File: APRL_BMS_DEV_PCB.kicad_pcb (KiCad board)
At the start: 4 copper layers, 73 parts, among them J1 Conn_01x04_Pin, J3 Conn_01x02_Pin, J4 Conn_01x08_Pin, J5 Conn_01x01_Pin, Q2 NPN, SW1 SW_SPDT, U1 BQ756506-Q1, U2 STM32F446RCTx, U3 ISO7741DWR, Y1 20MHz

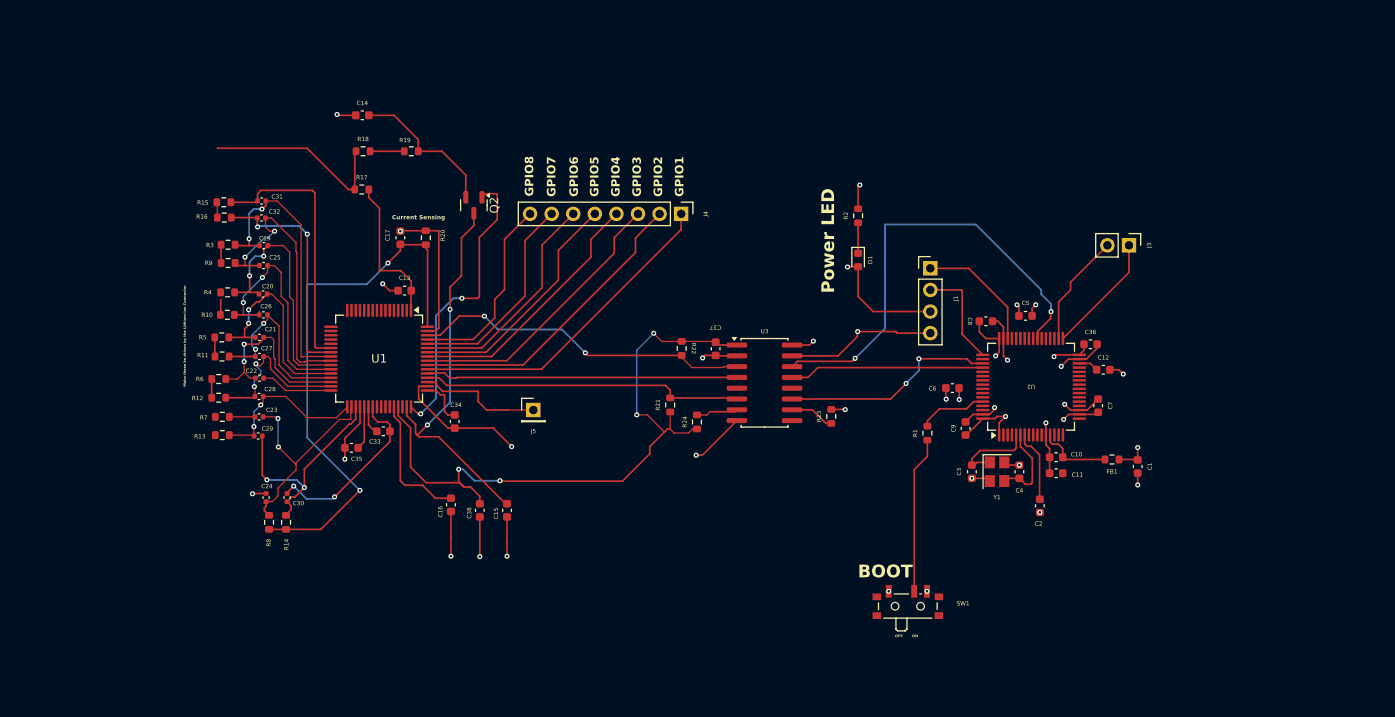
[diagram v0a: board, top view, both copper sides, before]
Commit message: Fixed silkscreen
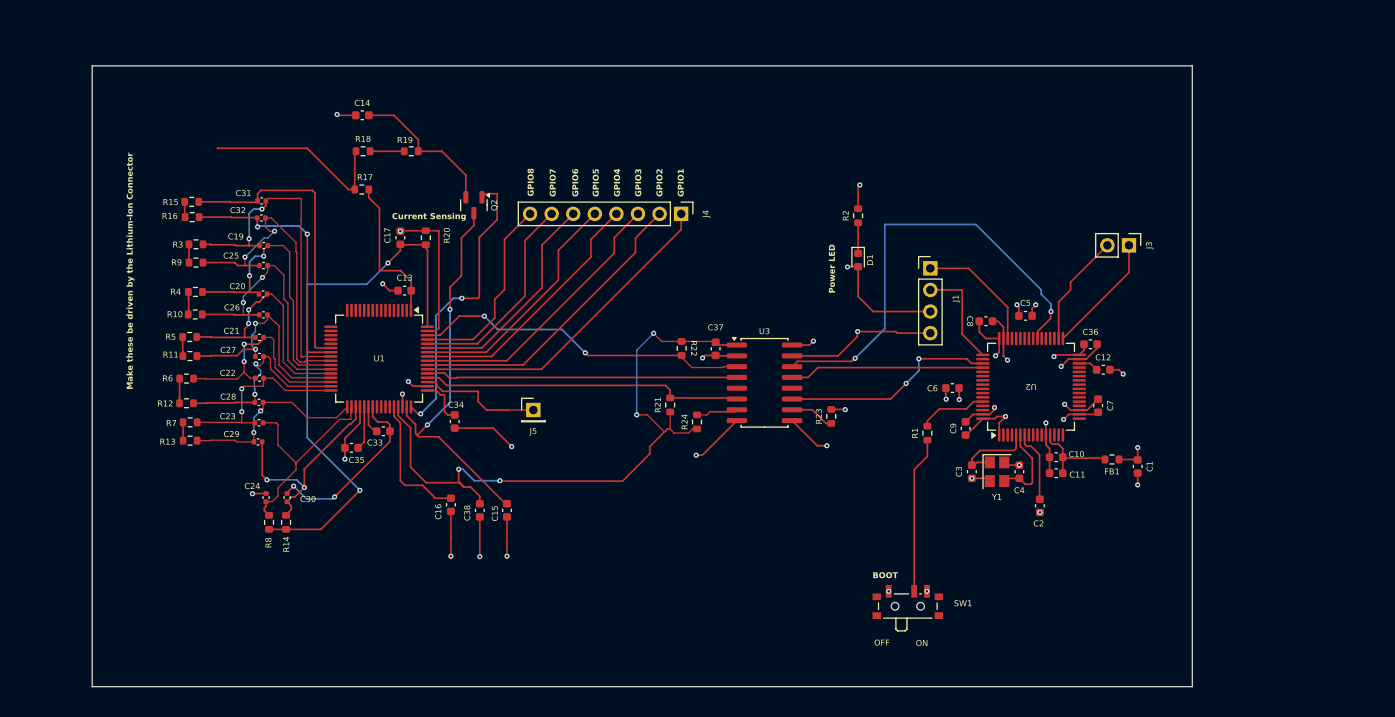
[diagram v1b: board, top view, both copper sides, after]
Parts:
- moved R12 3.85 mm to (87.7, 95.2)
- moved R13 3.85 mm to (88.1, 99.7)
- moved R7 3.85 mm to (88.1, 97.5)
- moved R10 3.78 mm to (88.7, 84.8)
- moved R11 3.78 mm to (88.1, 89.7)
- moved R15 3.78 mm to (88.3, 71.5)
- moved R16 3.78 mm to (88.4, 73.3)
- moved R3 3.78 mm to (88.8, 76.5)
- moved R4 3.78 mm to (88.8, 82.2)
- moved R5 3.78 mm to (88.1, 87.5)
- moved R6 3.78 mm to (87.7, 92.3)
- moved R9 3.78 mm to (88.8, 78.7)
- moved C23 0.70 mm to (96.2, 97.5)
- moved C28 0.70 mm to (96.2, 95.2)
- moved C29 0.70 mm to (96.1, 99.8)
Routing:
- net /CB1: track 11.5 -> 23.0 mm, vias 0 -> 2
- net /CB5: track 34.0 -> 39.8 mm
- net /VC2: track 20.2 -> 24.9 mm
- net /VC3: track 22.1 -> 26.8 mm
- net /CB2: track 22.2 -> 26.0 mm
- net /VC6: track 27.1 -> 30.9 mm
- net /CB4: track 30.4 -> 34.2 mm
- net /CB3: track 24.8 -> 28.6 mm
- net /CB6: track 31.1 -> 34.9 mm
- net /VC1: track 19.5 -> 23.2 mm
- net /VC4: track 28.4 -> 31.8 mm
- net /VC5: track 34.7 -> 37.7 mm
- net /CELL_1: track 0.00 -> 2.15 mm
- net +3.3VA: track 9.12 -> 11.0 mm
- net GND: track 151.0 -> 152.1 mm, vias 28 -> 31
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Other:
- board outline added: 129.5 x 73 mm

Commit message: Initial design COMPLETE!
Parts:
- added U5: ~, Custom_Connectors:S7B-XH-A-1, F.Cu at (79.8, 84.8)
- moved C12 13.6 mm to (209.1, 90.3)
- moved C15 13.6 mm to (138.9, 106.8)
- moved C36 13.6 mm to (207.6, 87.3)
- moved C4 13.6 mm to (199.2, 102.3)
- moved C6 13.6 mm to (191.3, 92.4)
- moved D1 13.6 mm to (180.2, 77.3)
- moved FB1 13.6 mm to (210.1, 100.8)
- moved J1 13.6 mm to (188.7, 78.3)
- moved J3 13.6 mm to (212.1, 75.6)
- moved J5 13.6 mm to (142.0, 95.0)
- moved R2 13.6 mm to (180.2, 72.1)
- moved R24 13.6 mm to (161.3, 96.4)
- moved SW1 13.6 mm to (186.1, 117.8)
- moved U2 13.6 mm to (200.6, 92.3)
- moved Y1 13.6 mm to (196.6, 102.3)
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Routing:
- net /CELL_6: track 24.6 -> 80.3 mm
- net /CELL_0: track 65.5 -> 108.3 mm
- net /CELL_1: track 2.15 -> 20.6 mm
- net /CELL_2: track 2.90 -> 19.8 mm
- net /CELL_5: track 2.15 -> 18.8 mm
- net /CELL_4: track 2.63 -> 18.8 mm
- net /CELL_3: track 2.26 -> 17.8 mm
- net GND: track 152.1 -> 138.7 mm
- net /CB1: track 23.0 -> 34.4 mm
- net /VC1: track 23.2 -> 34.2 mm
- net /VC2: track 24.9 -> 35.4 mm
- net /CB0: track 25.9 -> 35.7 mm
- net /CB2: track 26.0 -> 35.2 mm
- net /VC0: track 26.5 -> 35.5 mm
- net /VC6: track 30.9 -> 39.8 mm
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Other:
- board size 129.5 x 73 mm -> 160 x 80.2 mm
- board text removed: "Make these be driven by the Lithium-Ion Connector"
